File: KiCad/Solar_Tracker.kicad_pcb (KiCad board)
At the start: 2 copper layers, 160 x 100 mm, 116 parts, among them J1 +48V, J10 AZJMP, J11 ELJMP, J12 AZ, J13 CONN_01X03, J2 HOLE, J3 HOLE, J4 EL, J5 HOLE, J6 HOLE, J7 CONN_01X05, J8 GPIO, J9 GPIO, Q1 BUK9M42-60E, Q2 BUK9M42-60E, Q3 BUK9M42-60E, Q4 BUK9M42-60E, Q5 BUK9M42-60E, Q6 BUK9M42-60E, Q7 BUK9M42-60E, Q8 BUK9M42-60E, U1 MER1S4805SC, U10 TLP291, U11 75LBC182, U12 A4927, U2 A4927, U3 Nano, U4 A4927, U5 A4927, U6 MER1S4805SC, U7 TLP291, U8 TLP291, U9 TLP291

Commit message: added planes and updates
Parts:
- moved Q2 4.06 mm to (104.1, 41.1)
- moved R17 3.97 mm to (161.5, 68.7)
- moved U5 3.97 mm to (155.7, 82.1)
- moved C16 3.97 mm to (151.4, 68.7)
- moved C17 3.97 mm to (144.6, 82.3)
- moved C18 3.97 mm to (147.9, 82.3)
- moved C19 3.97 mm to (155.2, 68.7)
- moved C20 3.97 mm to (147.6, 68.7)
- moved R16 3.97 mm to (164.5, 81.7)
- moved R22 3.97 mm to (158.3, 68.7)
- moved R24 3.97 mm to (148.6, 91.9)
- moved D7 3.97 mm to (164.5, 74.5)
- moved Q1 3.56 mm to (129.5, 42.2)
- moved Q4 3.56 mm to (104.1, 33.0)
- moved J4 3.56 mm to (113.8, 40.1)
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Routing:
- net GND: track 91.7 -> 268.3 mm
- net Net-(Q3-Pad4): track 3.84 -> 88.8 mm, vias 1 -> 2
- net ISO_PWR_DET: track 5.25 -> 83.3 mm, vias 1 -> 2
- net AZ_B: track 29.7 -> 106.6 mm, vias 1 -> 2
- net Net-(Q2-Pad4): track 2.70 -> 70.6 mm, vias 1 -> 2
- net (no net): track 0.00 -> 66.0 mm
- net Net-(Q6-Pad4): track 1.72 -> 62.1 mm, vias 1 -> 2
- net EL_B: track 35.4 -> 95.2 mm, vias 1 -> 2
- net EL_F: track 35.4 -> 84.8 mm, vias 1 -> 2
- net AZRTE: track 12.4 -> 59.6 mm, vias 0 -> 2
- net Net-(Q4-Pad4): track 2.83 -> 48.5 mm, vias 1 -> 2
- net Net-(Q5-Pad4): track 2.17 -> 41.2 mm, vias 1 -> 2
- net Net-(Q1-Pad4): track 2.70 -> 37.0 mm, vias 1 -> 2
- net Net-(R19-Pad2): track 1.15 -> 32.9 mm, vias 1 -> 2
- net AZ_F: track 28.1 -> 57.9 mm, vias 1 -> 2
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- added copper zone on B.Cu, net GND
- added copper zone on B.Cu, net GNDD

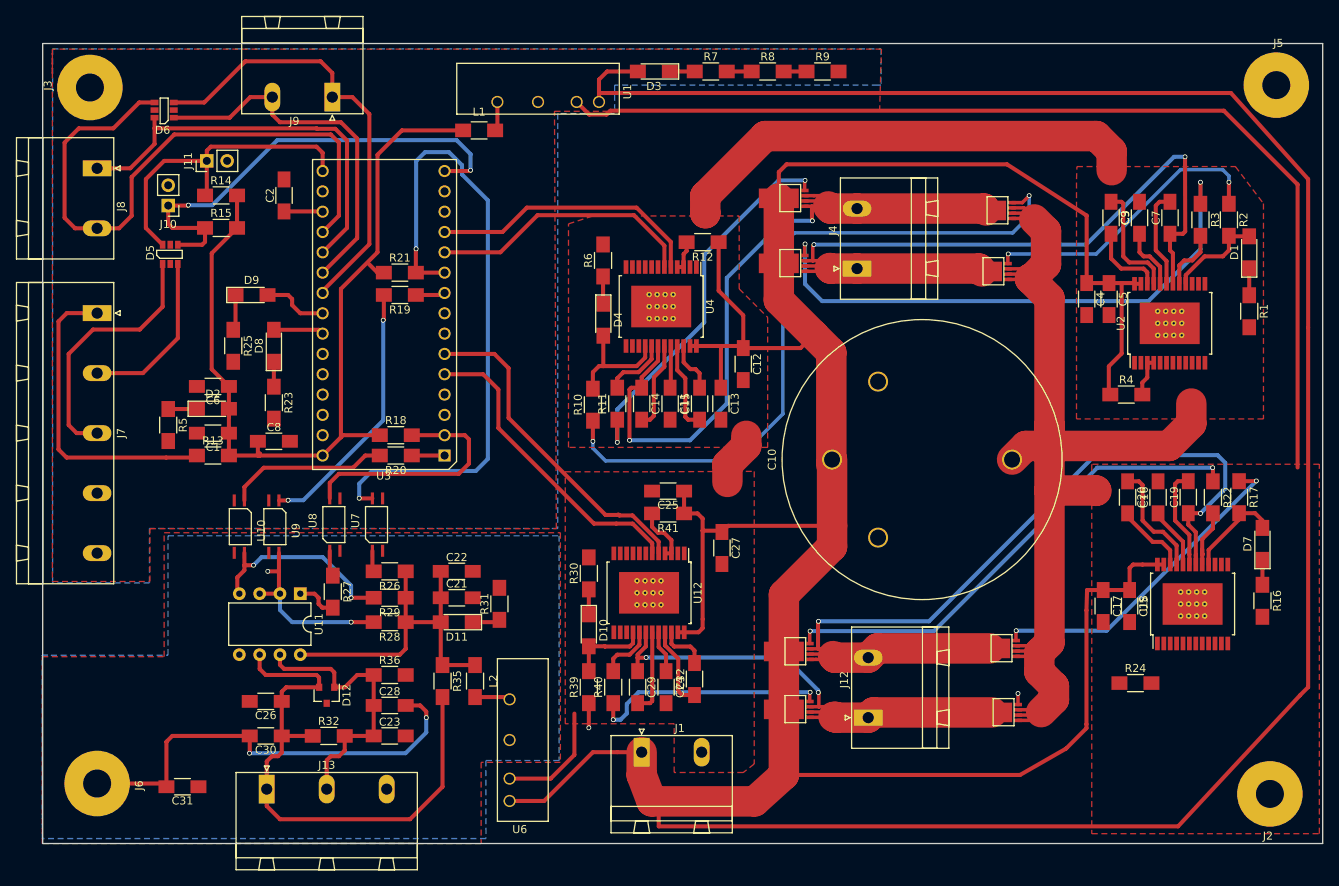
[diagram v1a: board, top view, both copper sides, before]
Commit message: silkscreen updates
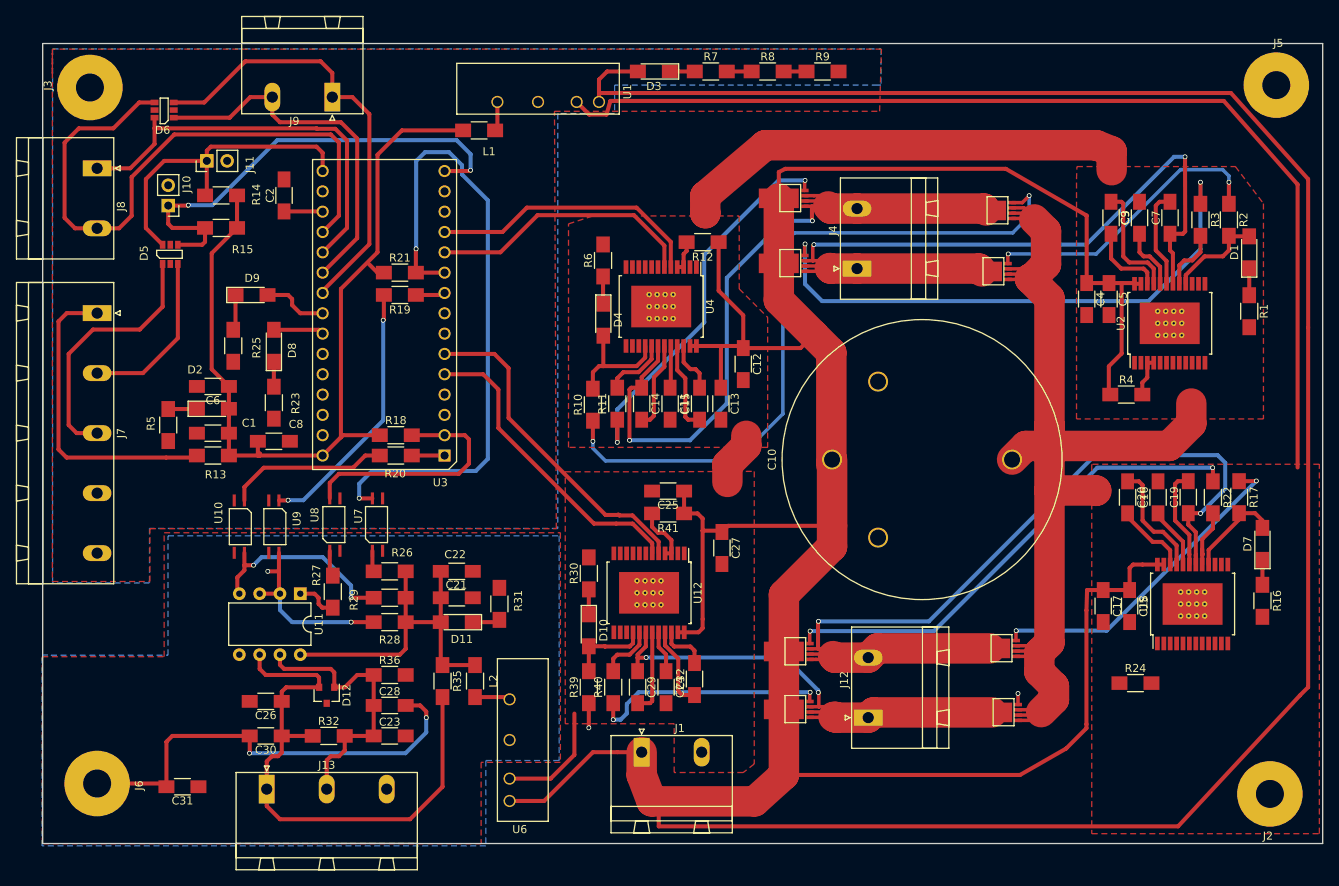
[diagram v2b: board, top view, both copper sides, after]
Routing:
- net GND: track 268.3 -> 270.3 mm
- net (no net): track 66.0 -> 64.6 mm
- net +48V: track 611.3 -> 610.7 mm

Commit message: added planes
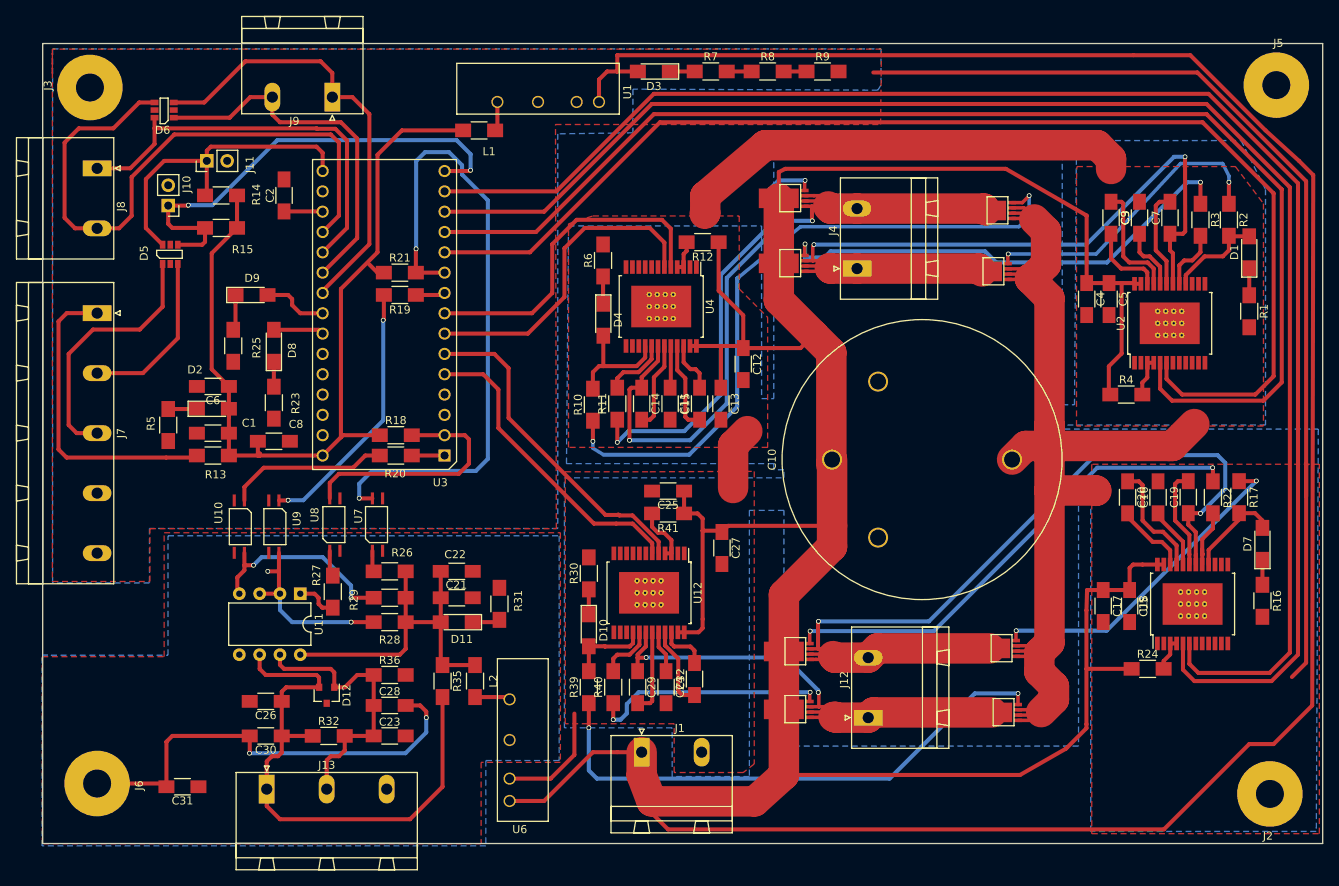
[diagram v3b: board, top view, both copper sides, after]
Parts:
- moved R24 2.34 mm to (150.1, 90.2)
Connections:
- U3 pad 11: ELFL -> ELBL
- U3 pad 12: ELFH -> ELBH
- U3 pad 13: ELBL -> AZBL
- U3 pad 14: ELBH -> AZBH
- U3 pad 7: AZBL -> ELFL
- U3 pad 8: AZBH -> ELFH
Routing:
- net AZBH: track 0.00 -> 194.9 mm
- net AZBL: track 0.00 -> 190.4 mm
- net ELBH: track 0.00 -> 158.8 mm
- net ELBL: track 0.00 -> 154.1 mm
- net Net-(Q7-Pad4): track 4.47 -> 68.3 mm
- net Net-(Q2-Pad4): track 70.6 -> 60.3 mm
- net ELFH: track 34.5 -> 42.0 mm
- net (no net): track 64.6 -> 57.3 mm
- net ELFL: track 33.7 -> 40.3 mm
- net +48V: track 610.7 -> 616.1 mm
- net Net-(R24-Pad2): track 0.00 -> 4.32 mm
- net Net-(Q4-Pad4): track 48.5 -> 52.6 mm
- net Net-(Q3-Pad4): track 88.8 -> 84.7 mm
- net Net-(Q1-Pad4): track 37.0 -> 38.2 mm

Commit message: updates
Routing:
- net (no net): track 57.3 -> 180.6 mm
- net GND: track 270.6 -> 165.3 mm, vias 0 -> 1
- net +48V: track 616.1 -> 614.2 mm, vias 0 -> 6
- net ELFL: track 40.3 -> 42.1 mm
- net ELFH: track 42.0 -> 43.7 mm
- net Net-(D1-Pad2): track 12.1 -> 13.7 mm

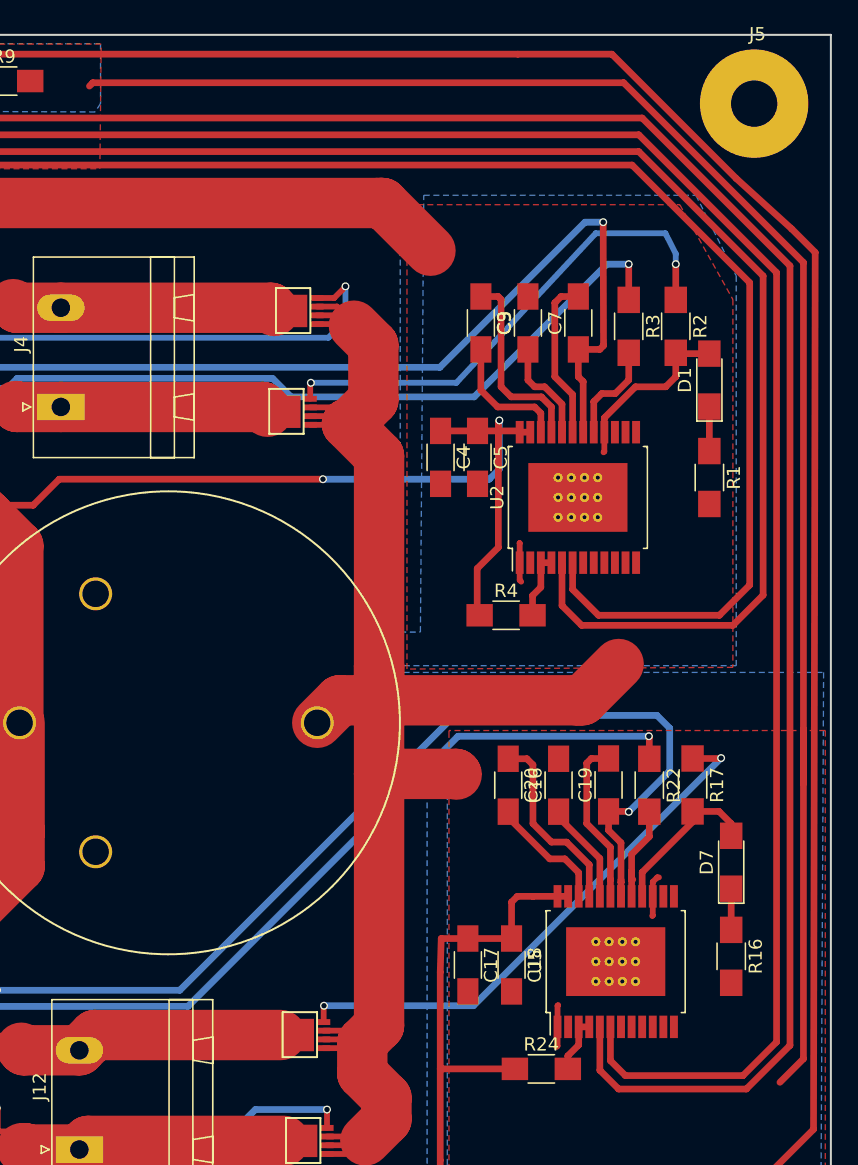
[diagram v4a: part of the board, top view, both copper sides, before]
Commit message: made the ratsnest go away
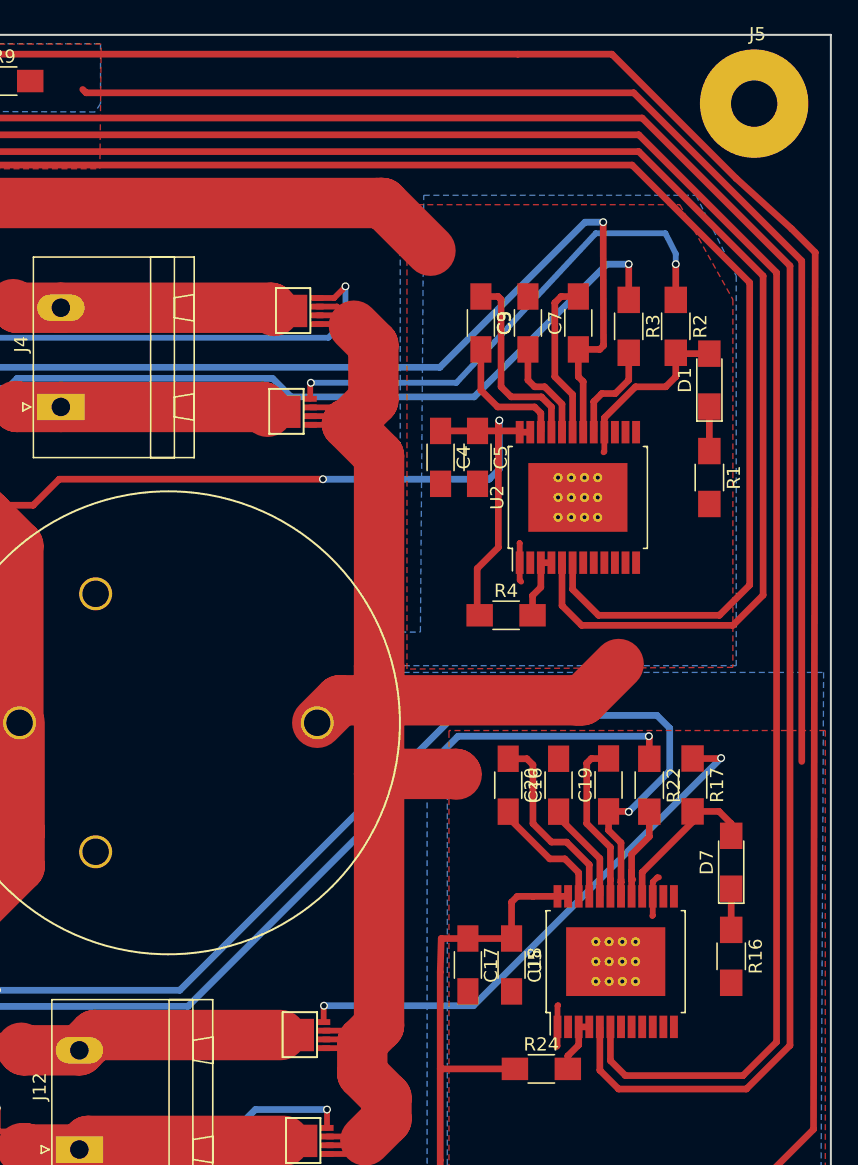
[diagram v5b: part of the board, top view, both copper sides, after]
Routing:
- net (no net): track 180.6 -> 59.5 mm
- net GND: track 165.3 -> 257.3 mm
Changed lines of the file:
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@@
     (thickness 1.6)
     (drawings 4)
-    (tracks 905)
+    (tracks 901)
     (zones 0)
     (modules 116)
@@
   (layers
     (0 F.Cu signal)
-    (31 B.Cu power hide)
+    (31 B.Cu power)
     (32 B.Adhes user)
     (33 F.Adhes user)
@@
   (segment (start 137.9982 24.7142) (end 138.1252 24.7142) (width 3.81) (layer F.Cu) (net 0))
   (segment (start 138.1252 24.7142) (end 141.732 28.321) (width 3.81) (layer F.Cu) (net 0))
-  (segment (start 156.337 15.621) (end 116.205 15.621) (width 0.508) (layer F.Cu) (net 0))
-  (segment (start 156.337 15.621) (end 169.926 29.21) (width 0.508) (layer F.Cu) (net 0))
-  (segment (start 169.926 68.58) (end 169.926 29.21) (width 0.508) (layer F.Cu) (net 0))
-  (segment (start 116.205 15.621) (end 115.951 15.875) (width 0.508) (layer F.Cu) (net 0))
   (segment (start 137.9982 24.7142) (end 137.9982 24.8412) (width 3.81) (layer F.Cu) (net 0))
-  (segment (start 169.926 64.516) (end 169.926 68.58) (width 0.508) (layer F.Cu) (net 0))
-  (segment (start 169.926 68.58) (end 169.926 89.408) (width 0.508) (layer F.Cu) (net 0))
-  (segment (start 169.926 89.408) (end 168.148 91.186) (width 0.508) (layer F.Cu) (net 0))
-  (segment (start 169.926 64.516) (end 169.926 64.77) (width 0.508) (layer F.Cu) (net 0))
+  (segment (start 97.282 61.722) (end 97.282 66.802) (width 3.81) (layer F.Cu) (net 0))
+  (segment (start 97.282 66.802) (end 97.663 67.183) (width 3.81) (layer F.Cu) (net 0))
   (segment (start 37.846 100.711) (end 57.3532 100.711) (width 0.508) (layer B.Cu) (net 1))
   (segment (start 37.878 98.552) (end 37.878 100.679) (width 0.508) (layer F.Cu) (net 1))
@@
   (segment (start 77.216 43.688) (end 77.216 37.592) (width 0.508) (layer F.Cu) (net 127))
   (segment (start 72.644 48.26) (end 77.216 43.688) (width 0.508) (layer F.Cu) (net 127))
-  (segment (start 28.378 20.32) (end 29.718 20.32) (width 0.508) (layer F.Cu) (net 132) (status 400000))
+  (segment (start 169.799 66.929) (end 169.799 29.083) (width 0.508) (layer F.Cu) (net 132))
+  (segment (start 115.697 16.383) (end 115.443 16.129) (width 0.508) (layer F.Cu) (net 132))
+  (segment (start 157.099 16.383) (end 115.697 16.383) (width 0.508) (layer F.Cu) (net 132))
+  (segment (start 169.799 29.083) (end 157.099 16.383) (width 0.508) (layer F.Cu) (net 132))
+  (segment (start 28.378 20.32) (end 29.718 20.32) (width 0.508) (layer F.Cu) (net 132))
   (via (at 29.718 20.32) (size 0.6) (drill 0.4) (layers F.Cu B.Cu) (net 132))
-  (segment (start 25.978 20.32) (end 28.378 20.32) (width 0.508) (layer F.Cu) (net 132) (status C00000))
-  (segment (start 27.94 39.554) (end 27.94 37.154) (width 0.508) (layer F.Cu) (net 132) (status C00000))
-  (segment (start 27.94 40.386) (end 27.94 39.554) (width 0.508) (layer F.Cu) (net 132) (status 800000))
-  (segment (start 27.94 36.195) (end 27.94 37.154) (width 0.508) (layer F.Cu) (net 132) (status 800000))
-  (segment (start 97.282 61.722) (end 97.282 66.802) (width 3.81) (layer F.Cu) (net 132))
-  (segment (start 97.282 66.802) (end 97.663 67.183) (width 3.81) (layer F.Cu) (net 132))
-  (segment (start 86.5115 49.808) (end 86.5115 48.4115) (width 0.508) (layer F.Cu) (net 132) (status 400000))
+  (segment (start 25.978 20.32) (end 28.378 20.32) (width 0.508) (layer F.Cu) (net 132))
+  (segment (start 27.94 39.554) (end 27.94 37.154) (width 0.508) (layer F.Cu) (net 132))
+  (segment (start 27.94 40.386) (end 27.94 39.554) (width 0.508) (layer F.Cu) (net 132))
+  (segment (start 27.94 36.195) (end 27.94 37.154) (width 0.508) (layer F.Cu) (net 132))
+  (segment (start 86.5115 49.808) (end 86.5115 48.4115) (width 0.508) (layer F.Cu) (net 132))
   (segment (start 158.877 75.692) (end 159.004 75.692) (width 0.44) (layer F.Cu) (net 132))
   (segment (start 158.535 76.034) (end 158.877 75.692) (width 0.44) (layer F.Cu) (net 132))
